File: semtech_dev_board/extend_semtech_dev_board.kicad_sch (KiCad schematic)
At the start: 0 parts

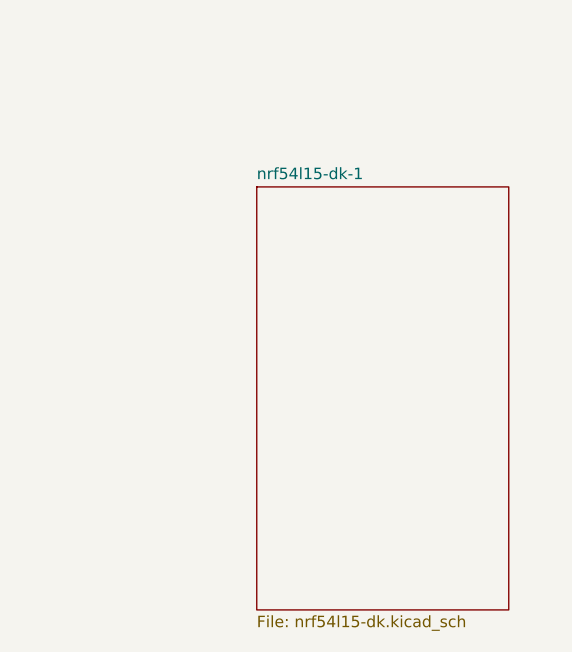
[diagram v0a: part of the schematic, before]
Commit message: starting point of design block
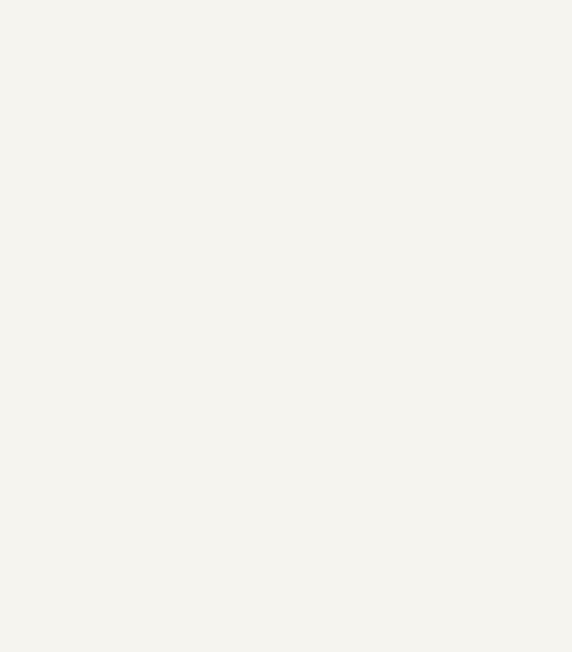
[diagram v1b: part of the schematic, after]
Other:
- removed sheet nrf54l15-dk-1
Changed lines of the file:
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@@
 	(generator_version "10.0")
 	(paper "A4")
-	(group "nrf54l15-dk"
-		(lib_id "Library:nrf54l15-dk")
-		(members "a0027f2f-e483-4d38-964c-a2b486088825")
-	)
 	(sheet
 		(at 38.31 33.34)
@@
 				)
 			)
-		)
-	)
-	(sheet
-		(at 139 59)
-		(size 28 47)
-		(exclude_from_sim no)
-		(in_bom yes)
-		(on_board yes)
-		(dnp no)
-		(fields_autoplaced yes)
-		(stroke
-			(width 0.1524)
-			(type solid)
-		)
-		(fill
-			(color 0 0 0 0)
-		)
-		(property "Sheetname" "nrf54l15-dk-1"
-			(at 139 58.2884 0)
-			(show_name no)
-			(do_not_autoplace no)
-			(effects
-				(font
-					(size 1.27 1.27)
-				)
-				(justify left bottom)
-			)
-		)
-		(property "Sheetfile" "nrf54l15-dk.kicad_sch"
-			(at 139 106.5846 0)
-			(show_name no)
-			(do_not_autoplace no)
-			(effects
-				(font
-					(size 1.27 1.27)
-				)
-				(justify left top)
-			)
-		)
-		(instances
-			(project "extend_semtech_dev_board"
-				(path "/8f61a2c4-0847-49da-a11e-89393006b40d"
-					(page "3")
-				)
-			)

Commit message: [fab] complete the design of semtech dev board
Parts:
- added C1, C2: 10u, Capacitor_SMD:C_1206_3216Metric, symbol Device:C_Small
- added C4, C5: 1u, Capacitor_SMD:C_0603_1608Metric, symbol Device:C_Small
- added C6: 100n, Capacitor_SMD:C_0603_1608Metric, symbol Device:C_Small
- added JP1, JP2, JP3: Jumper_2_Bridged, Connector_PinHeader_2.54mm:PinHeader_1x02_P2.54mm_Vertical, symbol Jumper:Jumper_2_Bridged
- added JP4: Jumper_3_Bridged12, Connector_PinHeader_2.54mm:PinHeader_1x03_P2.54mm_Vertical, symbol Jumper:Jumper_3_Bridged12
- added RF1, RF2: BWSMA-KWE-Z001, lcsc_footprints:C496551_SMA-TH_BWSMA-KWE-Z001, symbol lcsc_imported:BWSMA-KWE-Z001
- added U2: E80-900M2212S_C55338904, lcsc_footprints:C55338904_WIRELM-SMD_E80-900M2212S, symbol lcsc_imported:E80-900M2212S_C55338904
- added U3: E220-900M22S, lcsc_footprints:C2971736_WIRELM-SMD_22P-L20_0-W14_0-P1_27-BR, symbol lcsc_imported:E220-900M22S
- added U4: TLV75533PDBV, Package_TO_SOT_SMD:SOT-23-5, symbol Regulator_Linear:TLV75533PDBV
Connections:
- new net: U3.7 (TXEN), U3.8 (DIO2)
- new net +3V3: C2.2, C5.1, C6.1, U2.25 (VCC), U3.9 (VCC), U4.5 (OUT)
- new net +5V: C1.2, C4.1, JP4.3 (B), U4.1 (IN)
- new net EN: JP4.2 (C), U4.3 (EN)
- new net GND: C1.1, C2.1, C4.2, C5.2, C6.2, JP4.1 (A), RF1.1, RF1.2, RF1.3, RF1.4, RF2.1, RF2.2, RF2.3, RF2.4, U2.1 (GND), U2.11 (GND), U2.13 (GND), U2.14 (GND), U2.16 (GND), U2.19 (GND), U2.26 (GND), U2.8 (GND), U3.1 (GND), U3.10 (GND), U3.11 (GND), U3.12 (GND), U3.2 (GND), U3.20 (GND), U3.22 (GND), U3.3 (GND), U3.4 (GND), U4.2 (GND)
- new net HF: RF2.5, U2.12 (ANT)
- new net LF: RF1.5, U2.15 (ANT), U3.21 (ANT)
- new net NRST: U2.21 (LR_NRESET), U3.15 (NRST)
- new net P1.08/DIO: JP1.2 (B), U2.23 (DIO8), U3.13 (DIO1)
- new net P1.09/DIO: JP2.2 (B), U2.22 (DIO9), U3.5 (DIO3)
- new net P1.10/DIO/RXEN: JP3.2 (B), U2.24 (DIO7), U3.6 (RXEN)
- new net nrf54l15-dk/P0.00: U2.7 (BUSY), U3.14 (BUSY)
- new net nrf54l15-dk/P1.08: JP1.1 (A)
- new net nrf54l15-dk/P1.09: JP2.1 (A)
- new net nrf54l15-dk/P1.10: JP3.1 (A)
- new net nrf54l15-dk/P2.06: U2.5 (SCK), U3.18 (SCK)
- new net nrf54l15-dk/P2.08: U2.4 (MOSI), U3.17 (MOSI)
- new net nrf54l15-dk/P2.09: U2.3 (MISO), U3.16 (MISO)
- new net nrf54l15-dk/P2.10: U2.6 (NSS), U3.19 (NSS)
- no-connect marks 0 -> 4
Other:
- sheet nrf54l15-dk ports: added P0.00, P1.08, P1.09, P1.10, P2.06, P2.07, P2.08, P2.09, P2.10; removed none
